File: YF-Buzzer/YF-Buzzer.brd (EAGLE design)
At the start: 100 x 100 mm, 24 parts, among them IC1 74HC595N, IC2 74HC595N, IC3 74HC595N, IC4 74HC595N, IC5 74HC595N, IC6 74HC595N, IC7 74150N

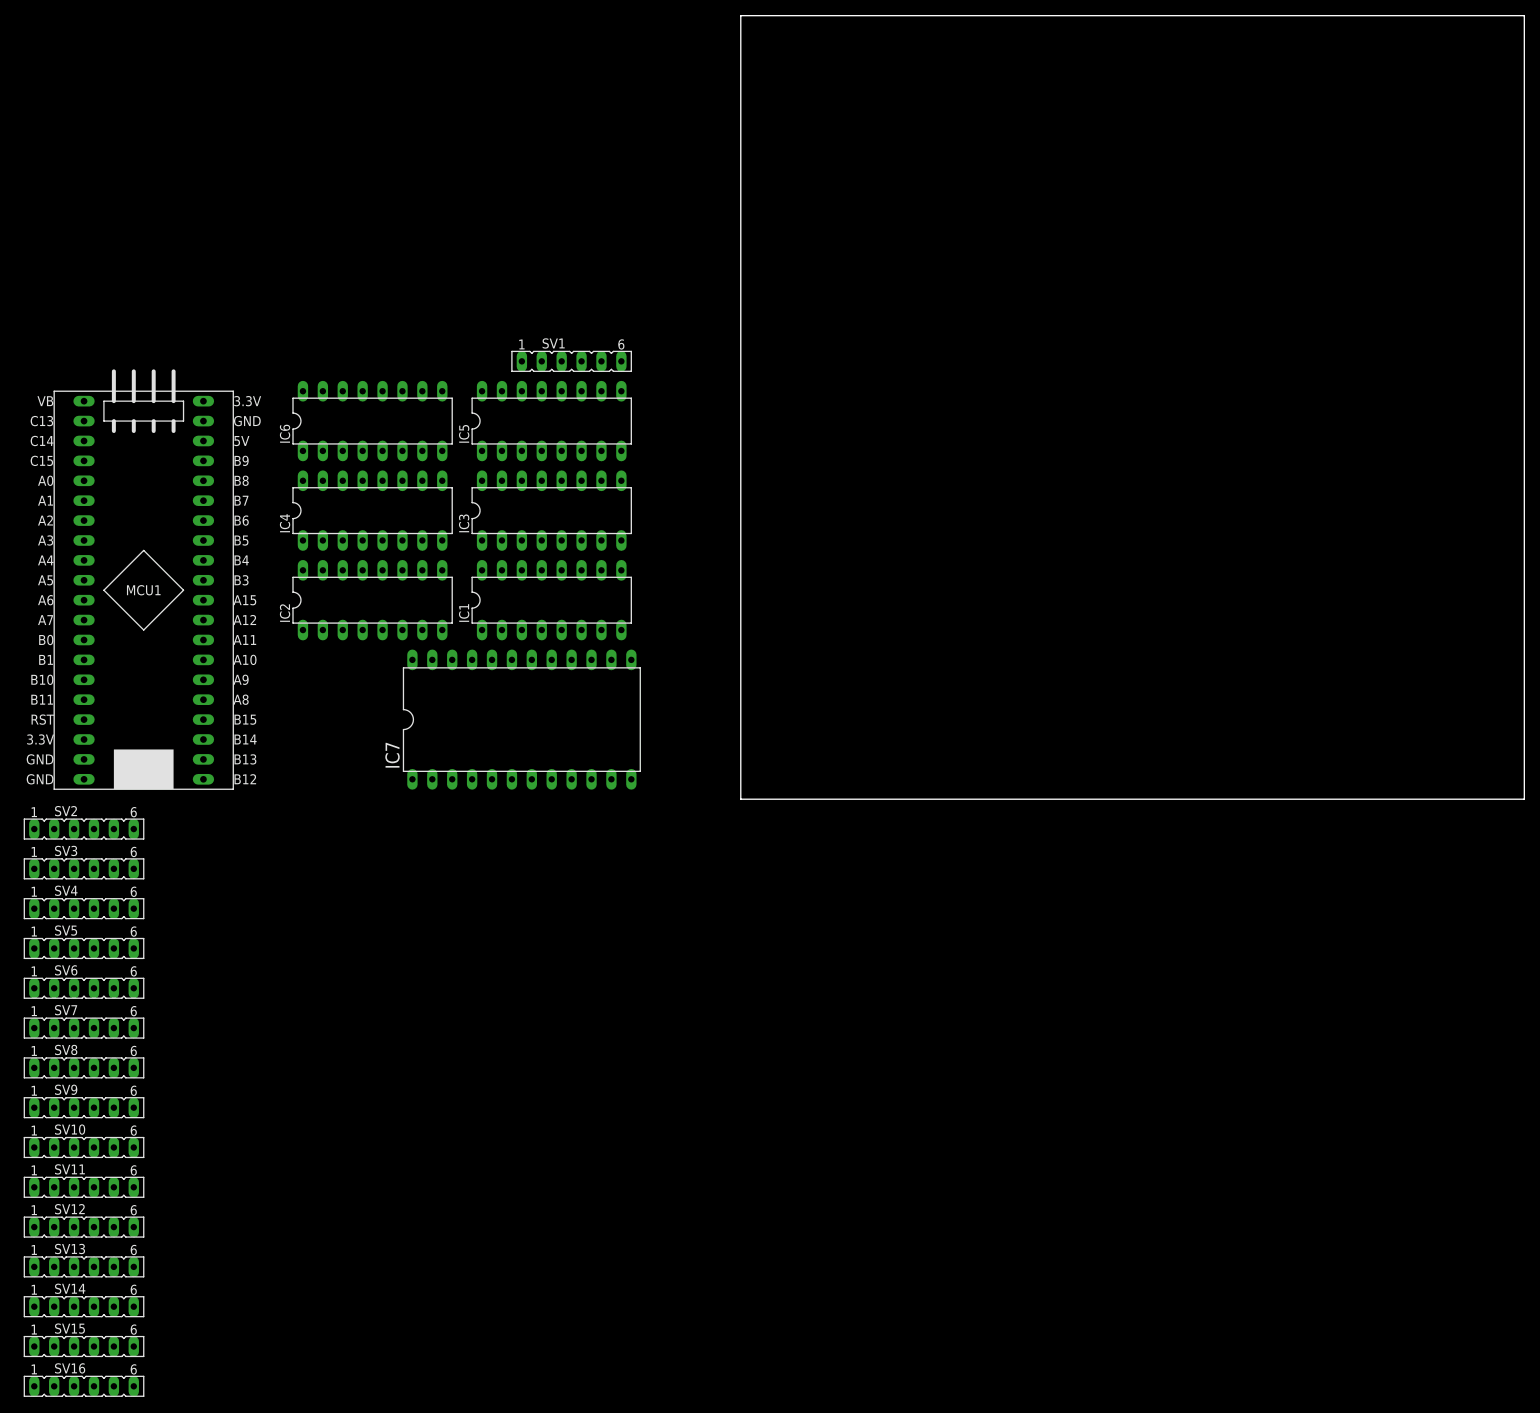
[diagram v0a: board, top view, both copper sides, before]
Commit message: Finished the shift register circuits and began layout of the PCB.
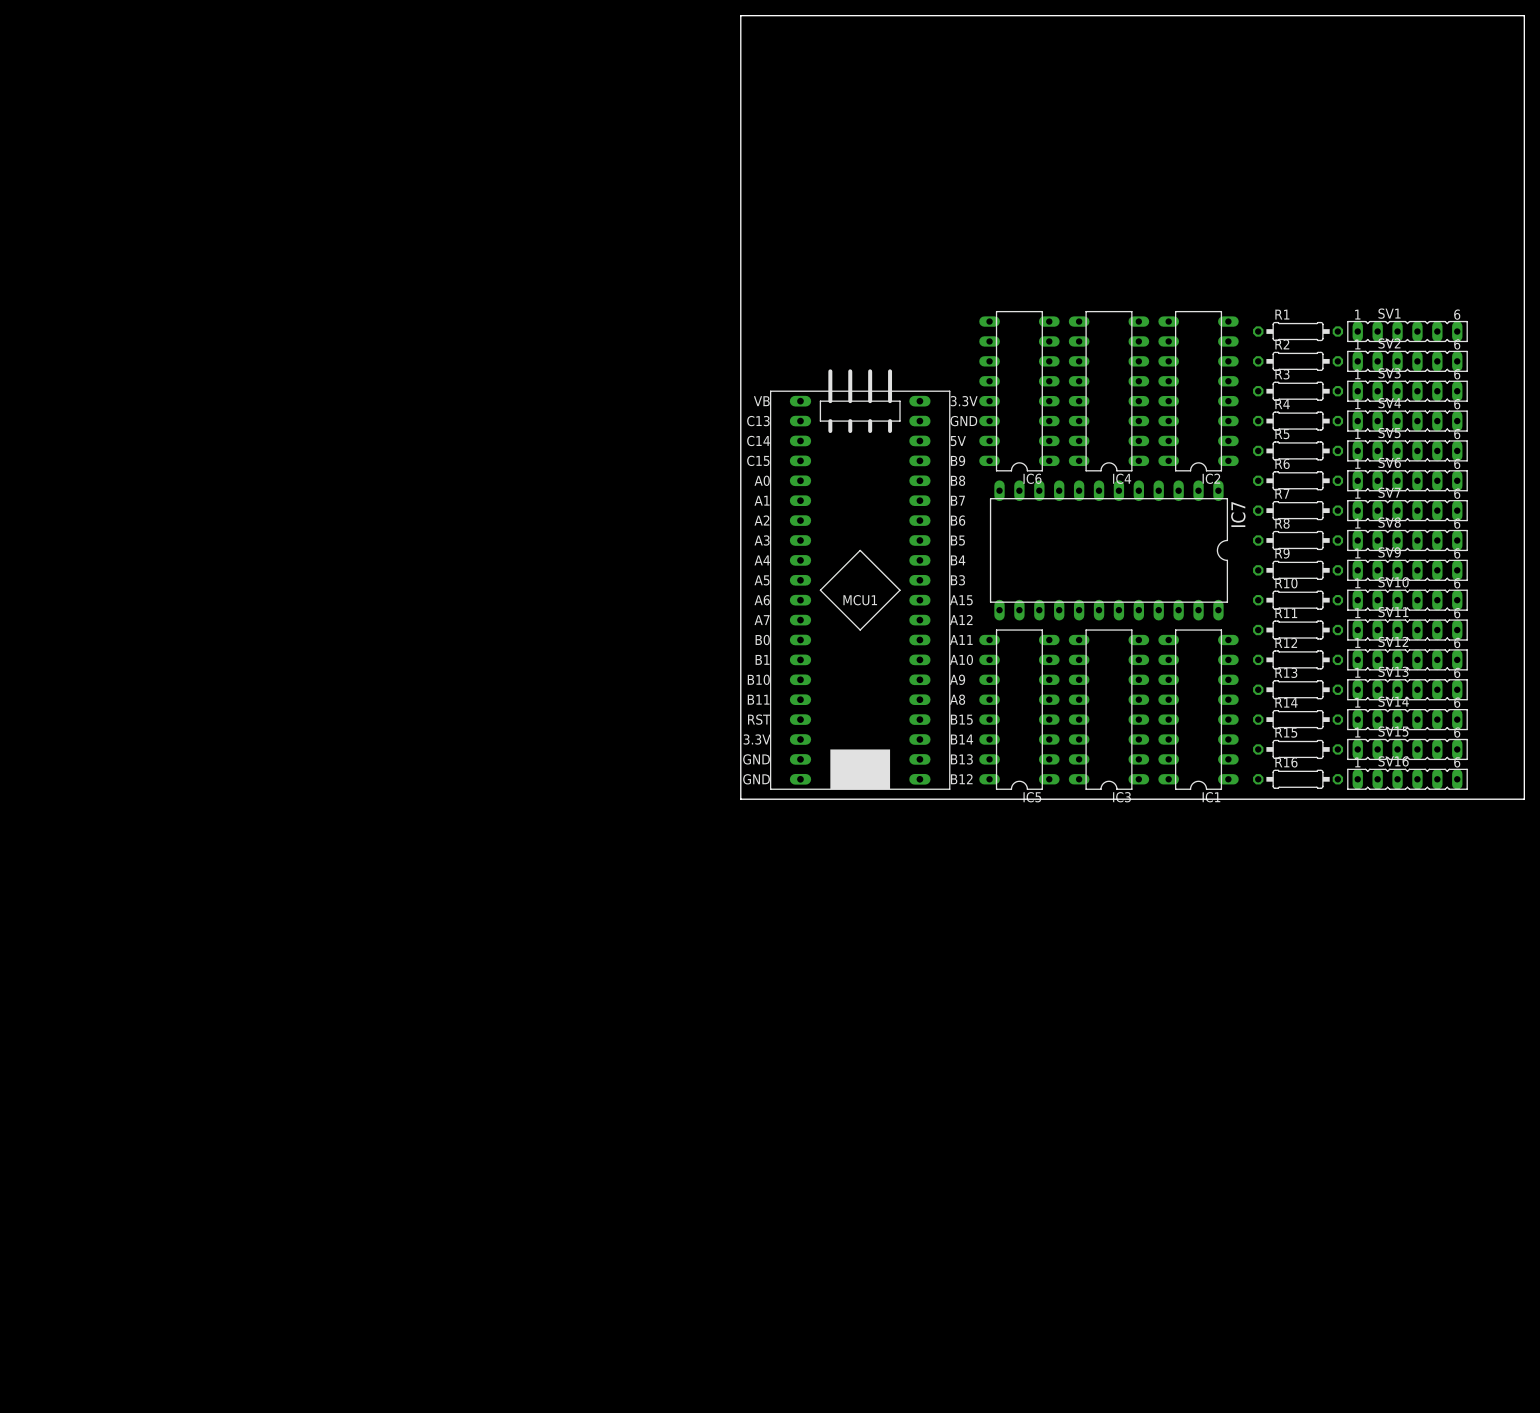
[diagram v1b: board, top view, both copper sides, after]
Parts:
- added R1, R10, R11, R12, R13, R14, R15, R16, R2, R3, R4, R5, R6, R7, R8, R9: 1K, rcl:0207/10
- moved SV16 185.8 mm to (85.1, 2.54)
- moved SV15 185.3 mm to (85.1, 6.35)
- moved SV14 184.8 mm to (85.1, 10.2)
- moved SV13 184.3 mm to (85.1, 14.0)
- moved SV12 183.8 mm to (85.1, 17.8)
- moved SV11 183.3 mm to (85.1, 21.6)
- moved SV10 182.8 mm to (85.1, 25.4)
- moved SV9 182.3 mm to (85.1, 29.2)
- moved SV8 181.8 mm to (85.1, 33.0)
- moved SV7 181.4 mm to (85.1, 36.8)
- moved SV6 180.9 mm to (85.1, 40.6)
- moved SV5 180.5 mm to (85.1, 44.5)
- moved SV4 180.0 mm to (85.1, 48.3)
- moved SV3 179.6 mm to (85.1, 52.1)
- moved SV2 179.1 mm to (85.1, 55.9)
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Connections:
- removed net 5V: MCU1.5V
- removed net GND1: MCU1.G1
- removed net GND2: MCU1.G2
- removed net GND3: MCU1.G3
- removed net N$10: SV2.5
- removed net N$11: SV1.5
- removed net N$12: SV1.4
- removed net N$13: SV1.3
- removed net N$14: SV1.2
- removed net N$15: SV1.1
- removed net N$16: SV5.5
- removed net N$17: SV5.4
- removed net N$18: SV2.4
- removed net N$19: SV2.3
- removed net N$20: SV2.2
- removed net N$21: SV2.1
- removed net N$22: SV3.5
- removed net N$23: SV3.4
- removed net N$24: SV3.3
- removed net N$25: SV3.2
- removed net N$26: SV3.1
- removed net N$27: SV4.5
- removed net N$28: SV4.4
- removed net N$29: SV4.3
- removed net N$30: SV4.2
- removed net N$31: SV4.1
- removed net N$32: SV5.3
- removed net N$33: SV5.2
- removed net N$34: SV5.1
- removed net N$35: SV6.5
- removed net N$36: SV6.4
- removed net N$37: SV6.3
- removed net N$38: SV6.2
- removed net N$39: SV6.1
- removed net N$4: IC5.11, IC6.11
- removed net N$40: SV7.5
- removed net N$41: SV7.4
- removed net N$42: SV7.3
- removed net N$43: SV7.2
- removed net N$44: SV7.1
- removed net N$45: SV8.5
- removed net N$46: SV8.4
- removed net N$47: SV8.3
- removed net N$48: SV8.2
- removed net N$49: SV8.1
- removed net N$5: IC1.12, IC2.12
- removed net N$50: SV9.5
- removed net N$51: SV9.4
- removed net N$52: SV9.3
- removed net N$53: SV9.2
- removed net N$54: SV9.1
- removed net N$55: SV10.5
- removed net N$56: SV10.4
- removed net N$57: SV10.3
- removed net N$58: SV10.2
- removed net N$59: SV10.1
- removed net N$6: IC3.11, IC4.11
- removed net N$60: SV11.5
- removed net N$61: SV11.4
- removed net N$62: SV11.3
- removed net N$63: SV11.2
- removed net N$64: SV11.1
- removed net N$65: SV12.5
- removed net N$66: SV12.4
- removed net N$67: SV12.3
- removed net N$68: SV12.2
- removed net N$69: SV12.1
- removed net N$7: IC3.12, IC4.12
- removed net N$70: SV13.5
- removed net N$71: SV13.4
- removed net N$72: SV13.3
- removed net N$73: SV13.2
- removed net N$74: SV13.1
- removed net N$75: SV14.5
- removed net N$76: SV14.4
- removed net N$77: SV14.3
- removed net N$78: SV14.2
- removed net N$79: SV14.1
- removed net N$8: IC1.11, IC2.11
- removed net N$80: SV15.5
- removed net N$81: SV15.4
- removed net N$82: SV15.3
- removed net N$83: SV15.2
- removed net N$84: SV15.1
- removed net N$85: SV16.5
- removed net N$86: SV16.4
- removed net N$87: SV16.3
- removed net N$88: SV16.2
- removed net N$89: SV16.1
- removed net N$9: IC5.12, IC6.12
- new net CLK: IC1.11, IC2.11, IC3.11, IC4.11, IC5.11, IC6.11, MCU1.B4
- new net DATA_LG: IC1.14, MCU1.A11
- new net DATA_LR: IC3.14, MCU1.A12
- new net DATA_LY: IC5.14, MCU1.A15
- new net LATCH: IC1.12, IC2.12, IC3.12, IC4.12, IC5.12, IC6.12, MCU1.B3
- new net LG0: IC2.7, SV1.6
- new net LG1: IC2.6, SV2.6
- new net LG10: IC1.5, SV11.6
- new net LG11: IC1.4, SV12.6
- new net LG12: IC1.3, SV13.6
- new net LG13: IC1.2, SV14.6
- new net LG14: IC1.1, SV15.6
- new net LG15: IC1.15, SV16.6
- new net LG2: IC2.5, SV3.6
- new net LG3: IC2.4, SV4.6
- new net LG4: IC2.3, SV5.6
- new net LG5: IC2.2, SV6.6
- new net LG6: IC2.1, SV7.6
- new net LG7: IC2.15, SV8.6
- new net LG8: IC1.7, SV9.6
- new net LG9: IC1.6, SV10.6
- new net LR0: IC4.7, SV1.5
- new net LR1: IC4.6, SV2.5
- new net LR10: IC3.5, SV11.5
- new net LR11: IC3.4, SV12.5
- new net LR12: IC3.3, SV13.5
- new net LR13: IC3.2, SV14.5
- new net LR14: IC3.1, SV15.5
- new net LR15: IC3.15, SV16.5
- new net LR2: IC4.5, SV3.5
- new net LR3: IC4.4, SV4.5
- new net LR4: IC4.3, SV5.5
- new net LR5: IC4.2, SV6.5
- new net LR6: IC4.1, SV7.5
- new net LR7: IC4.15, SV8.5
- new net LR8: IC3.7, SV9.5
- new net LR9: IC3.6, SV10.5
- new net LY0: IC6.7, SV1.2
- new net LY1: IC6.6, SV2.2
- new net LY10: IC5.5, SV11.2
- new net LY11: IC5.4, SV12.2
- new net LY12: IC5.3, SV13.2
- new net LY13: IC5.2, SV14.2
- new net LY14: IC5.1, SV15.2
- new net LY15: IC5.15, SV16.2
- new net LY2: IC6.5, SV3.2
- new net LY3: IC6.4, SV4.2
- new net LY4: IC6.3, SV5.2
- new net LY5: IC6.2, SV6.2
- new net LY6: IC6.1, SV7.2
- new net LY7: IC6.15, SV8.2
- new net LY8: IC5.7, SV9.2
- new net LY9: IC5.6, SV10.2
- new net MUX_A: IC7.15, MCU1.B12
- new net MUX_B: IC7.14, MCU1.B13
- new net MUX_C: IC7.13, MCU1.B14
- new net MUX_D: IC7.11, MCU1.B15
- new net MUX_IN: IC7.10, MCU1.A8
- net +5V: now also MCU1.5V, SV1.4, SV10.4, SV11.4, SV12.4, SV13.4, SV14.4, SV15.4, SV16.4, SV2.4, SV3.4, SV4.4, SV5.4, SV6.4, SV7.4, SV8.4, SV9.4
- net IN0: now also R1.2, SV1.1; no longer SV1.6
- net IN1: now also R2.2, SV2.1; no longer SV2.6
- net IN10: now also R11.2, SV11.1; no longer SV11.6
- net IN11: now also R12.2, SV12.1; no longer SV12.6
- net IN12: now also R13.2, SV13.1; no longer SV13.6
- net IN13: now also R14.2, SV14.1; no longer SV14.6
- net IN14: now also R15.2, SV15.1; no longer SV15.6
- net IN15: now also R16.2, SV16.1; no longer SV16.6
- net IN2: now also R3.2, SV3.1; no longer SV3.6
- net IN3: now also R4.2, SV4.1; no longer SV4.6
- net IN4: now also R5.2, SV5.1; no longer SV5.6
- net IN5: now also R6.2, SV6.1; no longer SV6.6
- net IN6: now also R7.2, SV7.1; no longer SV7.6
- net IN7: now also R8.2, SV8.1; no longer SV8.6
- net IN8: now also R9.2, SV9.1; no longer SV9.6
- net IN9: now also R10.2, SV10.1; no longer SV10.6
- net PE: now also IC7.9, MCU1.G1, MCU1.G2, MCU1.G3, R1.1, R10.1, R11.1, R12.1, R13.1, R14.1, R15.1, R16.1, R2.1, R3.1, R4.1, R5.1, R6.1, R7.1, R8.1, R9.1, SV1.3, SV10.3, SV11.3, SV12.3, SV13.3, SV14.3, SV15.3, SV16.3, SV2.3, SV3.3, SV4.3, SV5.3, SV6.3, SV7.3, SV8.3, SV9.3
